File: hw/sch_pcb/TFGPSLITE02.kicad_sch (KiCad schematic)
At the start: 27 parts, among them J1 SM06B-GHS-TB, J2 SM04B-GHS-TB, M1 HOLE, M2 HOLE, M3 HOLE, M4 HOLE, U1 MIC5504-3.3YM5, U2 SAM-M8Q

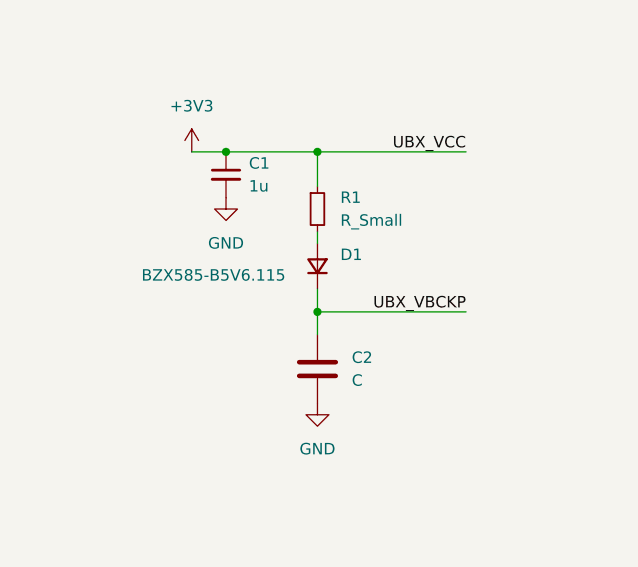
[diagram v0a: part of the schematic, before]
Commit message: Update schematics and PCB title blocks.
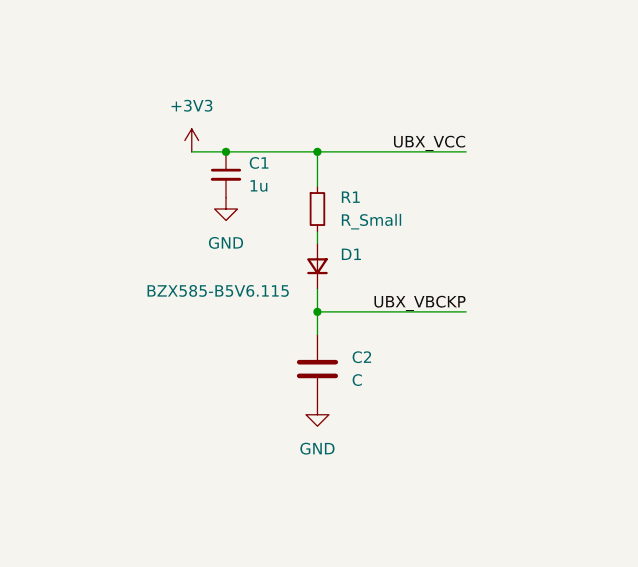
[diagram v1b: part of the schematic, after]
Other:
- company: (none) -> ThunderFly s.r.o.
- title: (none) -> TFGPSLITE02A
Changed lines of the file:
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@@
 	(generator_version "8.0")
 	(paper "A4")
+	(title_block
+		(title "TFGPSLITE02A")
+		(date "2025-01-11")
+		(rev "A")
+		(company "ThunderFly s.r.o.")
+		(comment 1 "Compact GNSS Module for\\nlightweight UAVs")
+	)
 	(junction
 		(at 105.41 29.21)
@@
 		)
 		(property "Value" "BZX585-B5V6.115"
-			(at 37.592 112.776 90)
-			(effects
-				(font
+			(at 38.1 114.554 90)
+			(effects
+				(font
